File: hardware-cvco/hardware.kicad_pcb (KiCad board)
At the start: 4 copper layers, 2 parts, among them J1 Conn_Coaxial, Y1 CVCO55

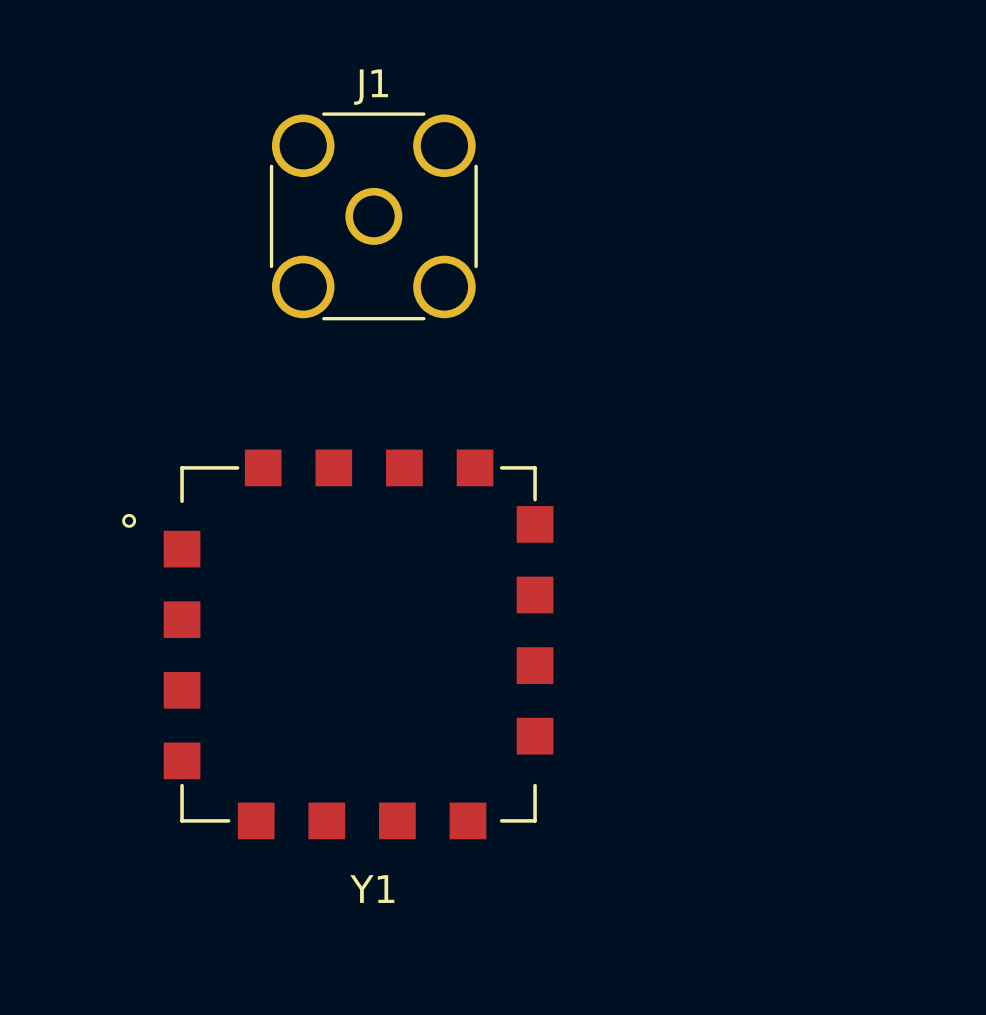
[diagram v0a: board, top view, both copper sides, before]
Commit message: 500-1000 MHz & 1000-2000 MHz Crystek VCOs.
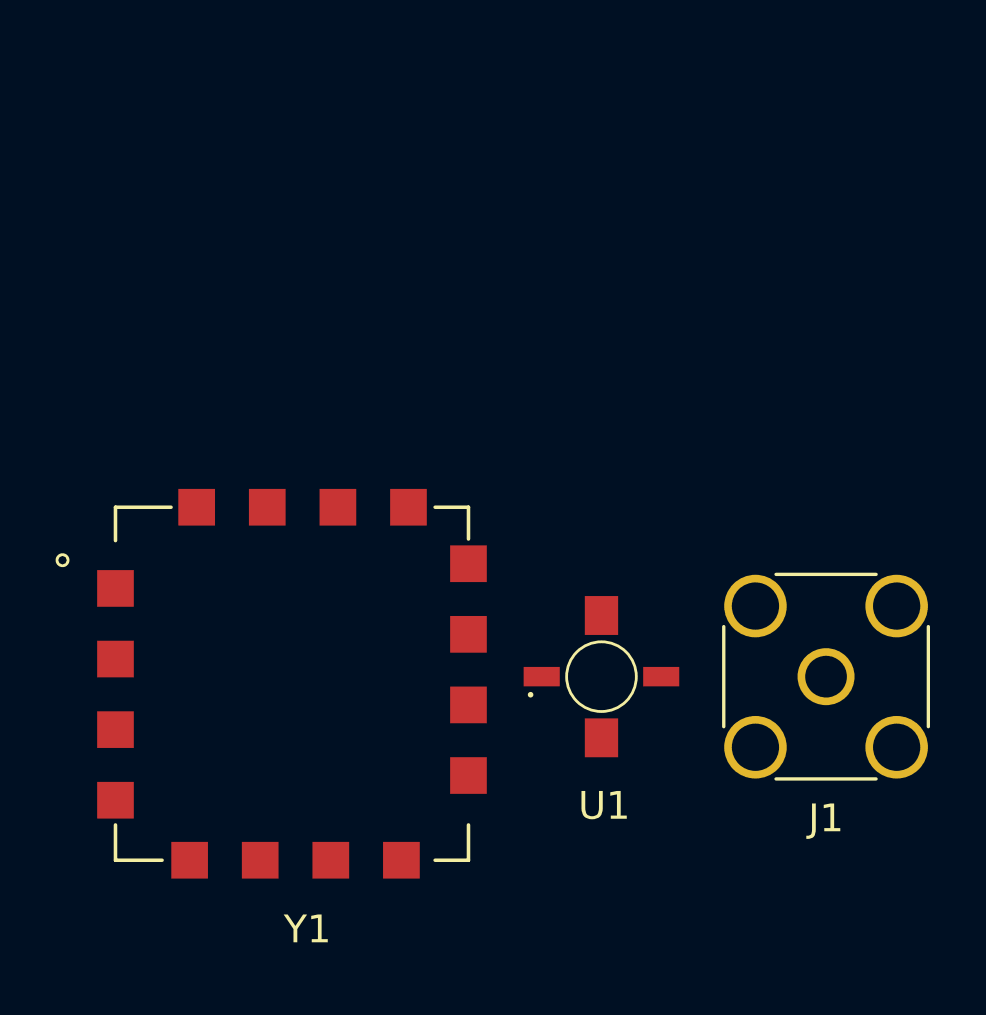
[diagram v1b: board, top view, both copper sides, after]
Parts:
- added U1: NLB-310-T1, CVCO:Micro-X-4, F.Cu at (131.4, 68.0)
- J1: value Conn_Coaxial -> SMA
- moved J1 23.2 mm to (139.5, 68.0), turned to 270 degrees
- moved Y1 2.78 mm to (113.9, 74.6)
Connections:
- J1 pad 2: Net-(J1-Pad2) -> GND
- Y1 pad 14: Net-(Y1-Pad14) -> GND

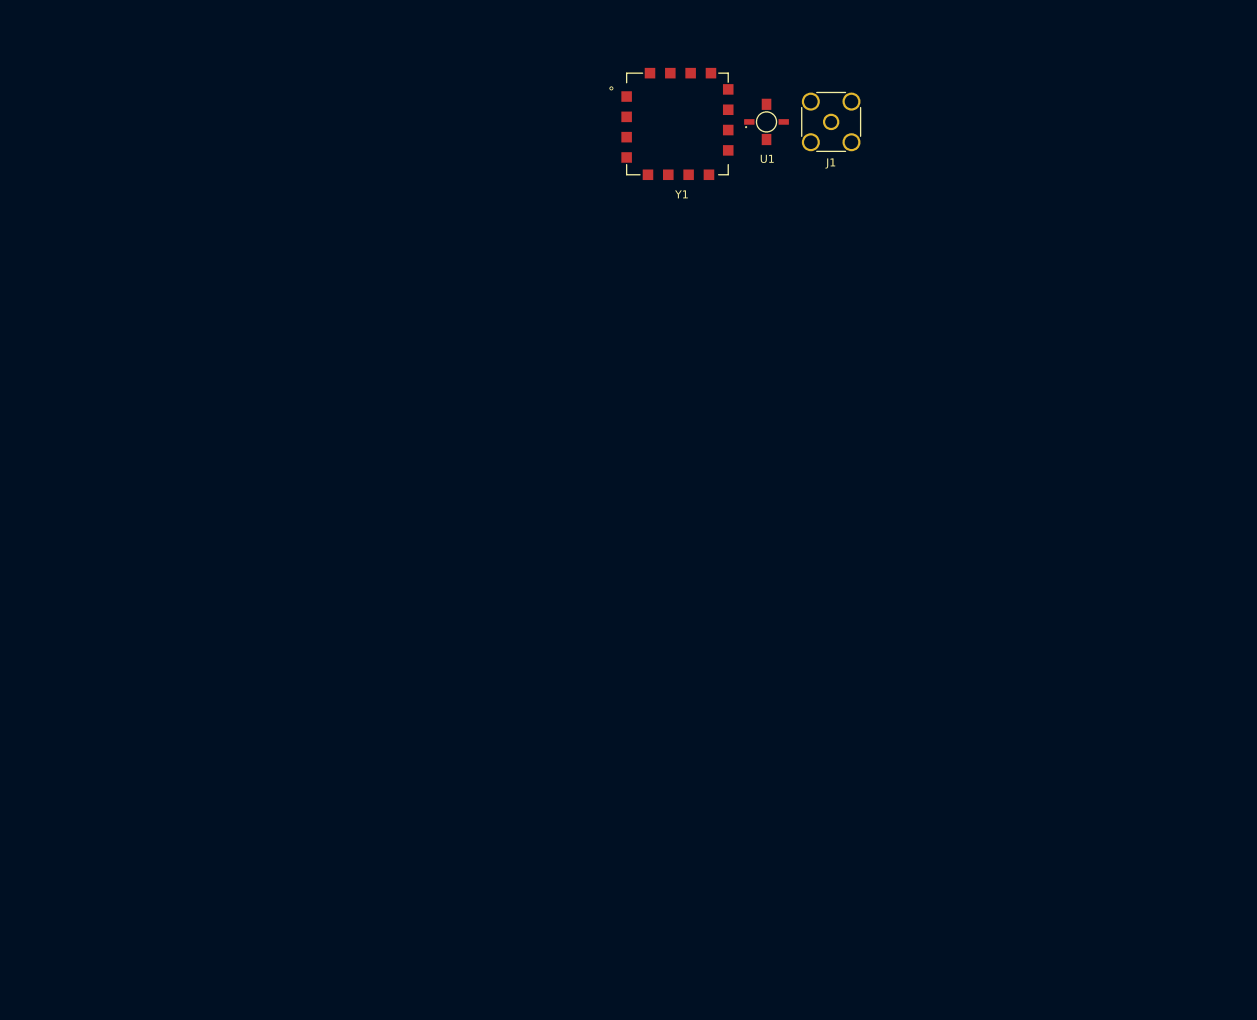
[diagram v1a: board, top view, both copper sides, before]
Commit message: Simplified CVCO design.
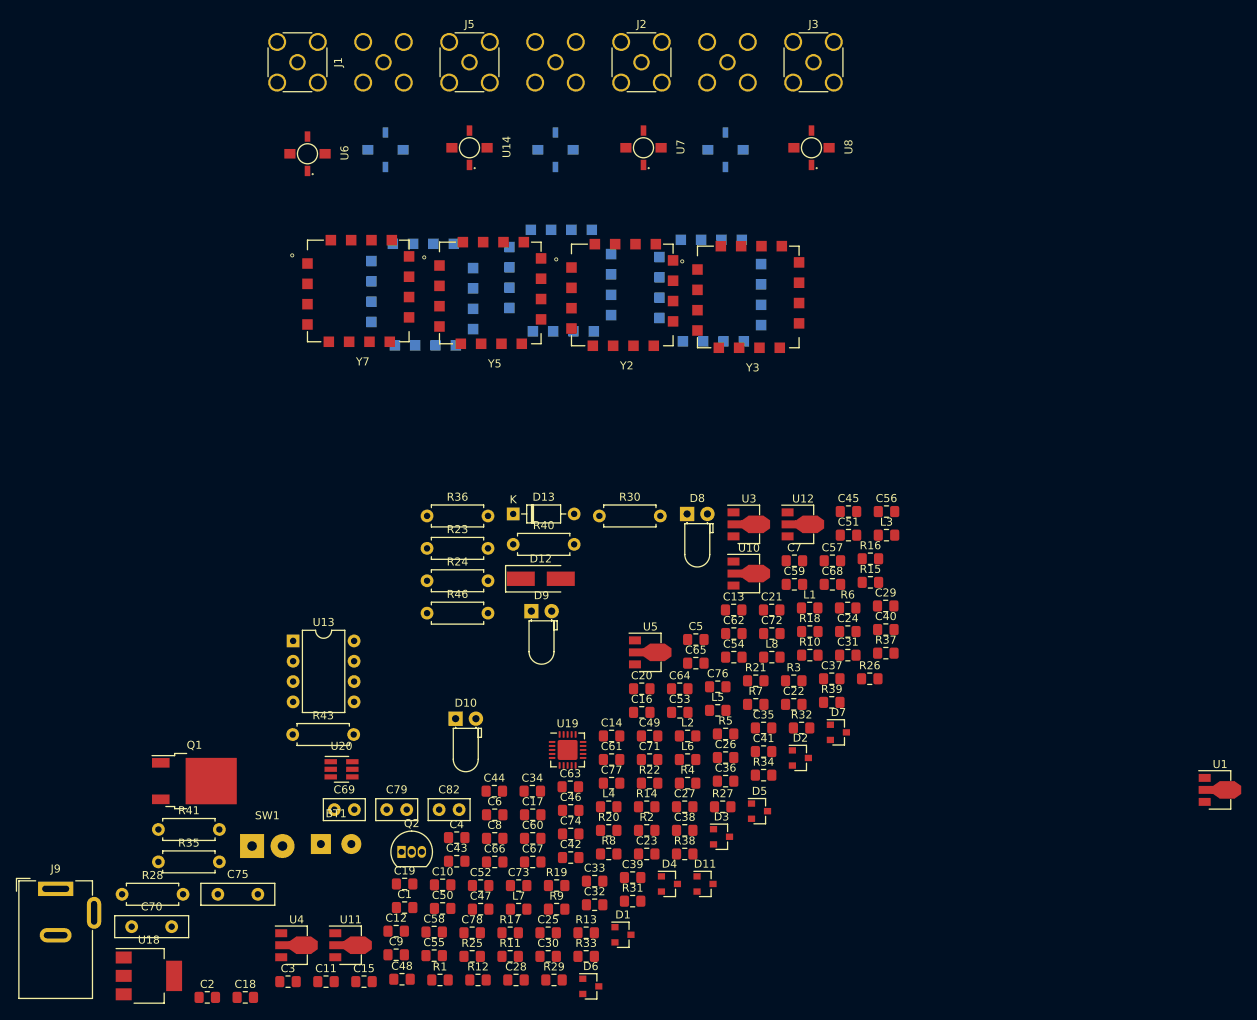
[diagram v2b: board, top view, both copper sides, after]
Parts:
- added BT1: 3.7V, Connector_Wire:SolderWirePad_1x02_P3.81mm_Drill1mm, F.Cu at (75.7, 158.3)
- added C1: 1μ, Capacitor_SMD:C_0805_2012Metric_Pad1.15x1.40mm_HandSolder, F.Cu at (86.1, 166.2)
- added C10: 0.1n, Capacitor_SMD:C_0805_2012Metric_Pad1.15x1.40mm_HandSolder, F.Cu at (90.9, 163.4)
- added C11: 1n, Capacitor_SMD:C_0805_2012Metric_Pad1.15x1.40mm_HandSolder, F.Cu at (76.3, 175.5)
- added C12: 0.1n, Capacitor_SMD:C_0805_2012Metric_Pad1.15x1.40mm_HandSolder, F.Cu at (85.1, 169.2)
- added C13: 1n, Capacitor_SMD:C_0805_2012Metric_Pad1.15x1.40mm_HandSolder, F.Cu at (127.3, 129.0)
- added C14: 0.1n, Capacitor_SMD:C_0805_2012Metric_Pad1.15x1.40mm_HandSolder, F.Cu at (112.0, 144.8)
- added C15: 1n, Capacitor_SMD:C_0805_2012Metric_Pad1.15x1.40mm_HandSolder, F.Cu at (81.1, 175.5)
- added C16: 0.1n, Capacitor_SMD:C_0805_2012Metric_Pad1.15x1.40mm_HandSolder, F.Cu at (115.8, 141.8)
- added C17: 0.1n, Capacitor_SMD:C_0805_2012Metric_Pad1.15x1.40mm_HandSolder, F.Cu at (102.2, 154.6)
- added C18: 1n, Capacitor_SMD:C_0805_2012Metric_Pad1.15x1.40mm_HandSolder, F.Cu at (66.2, 177.5)
- added C19: 0.1n, Capacitor_SMD:C_0805_2012Metric_Pad1.15x1.40mm_HandSolder, F.Cu at (86.1, 163.3)
- added C2: 0.1u, Capacitor_SMD:C_0805_2012Metric_Pad1.15x1.40mm_HandSolder, F.Cu at (61.5, 177.5)
- added C20: 1n, Capacitor_SMD:C_0805_2012Metric_Pad1.15x1.40mm_HandSolder, F.Cu at (115.8, 138.9)
- added C21: 0.1n, Capacitor_SMD:C_0805_2012Metric_Pad1.15x1.40mm_HandSolder, F.Cu at (132.0, 129.0)
- added C22: 1n, Capacitor_SMD:C_0805_2012Metric_Pad1.15x1.40mm_HandSolder, F.Cu at (134.8, 140.8)
- added C23: 0.1n, Capacitor_SMD:C_0805_2012Metric_Pad1.15x1.40mm_HandSolder, F.Cu at (116.4, 159.5)
- added C24: 1n, Capacitor_SMD:C_0805_2012Metric_Pad1.15x1.40mm_HandSolder, F.Cu at (141.5, 131.7)
- added C25: 470pF, Capacitor_SMD:C_0805_2012Metric_Pad1.15x1.40mm_HandSolder, F.Cu at (104.1, 169.4)
- added C26: 220pF, Capacitor_SMD:C_0805_2012Metric_Pad1.15x1.40mm_HandSolder, F.Cu at (126.3, 147.5)
- added C27: 100pF, Capacitor_SMD:C_0805_2012Metric_Pad1.15x1.40mm_HandSolder, F.Cu at (121.2, 153.6)
- added C28: 47pF, Capacitor_SMD:C_0805_2012Metric_Pad1.15x1.40mm_HandSolder, F.Cu at (100.1, 175.3)
- added C29: 1n, Capacitor_SMD:C_0805_2012Metric_Pad1.15x1.40mm_HandSolder, F.Cu at (146.3, 128.5)
- added C3: 1μ, Capacitor_SMD:C_0805_2012Metric_Pad1.15x1.40mm_HandSolder, F.Cu at (71.6, 175.5)
- added C30: 0.1n, Capacitor_SMD:C_0805_2012Metric_Pad1.15x1.40mm_HandSolder, F.Cu at (104.1, 172.3)
- added C31: 1n, Capacitor_SMD:C_0805_2012Metric_Pad1.15x1.40mm_HandSolder, F.Cu at (141.5, 134.7)
- added C32: 0.1n, Capacitor_SMD:C_0805_2012Metric_Pad1.15x1.40mm_HandSolder, F.Cu at (109.9, 165.9)
- added C33: 1n, Capacitor_SMD:C_0805_2012Metric_Pad1.15x1.40mm_HandSolder, F.Cu at (109.9, 162.9)
- added C34: 0.1n, Capacitor_SMD:C_0805_2012Metric_Pad1.15x1.40mm_HandSolder, F.Cu at (102.1, 151.7)
- added C35: 1n, Capacitor_SMD:C_0805_2012Metric_Pad1.15x1.40mm_HandSolder, F.Cu at (131.0, 143.8)
- added C36: 0.1n, Capacitor_SMD:C_0805_2012Metric_Pad1.15x1.40mm_HandSolder, F.Cu at (126.3, 150.4)
- added C37: 1μ, Capacitor_SMD:C_0805_2012Metric_Pad1.15x1.40mm_HandSolder, F.Cu at (139.5, 137.6)
- added C38: 0.1u, Capacitor_SMD:C_0805_2012Metric_Pad1.15x1.40mm_HandSolder, F.Cu at (121.2, 156.6)
- added C39: 1μ, Capacitor_SMD:C_0805_2012Metric_Pad1.15x1.40mm_HandSolder, F.Cu at (114.6, 162.5)
- added C4: 0.1u, Capacitor_SMD:C_0805_2012Metric_Pad1.15x1.40mm_HandSolder, F.Cu at (92.7, 157.5)
- added C40: 0.1u, Capacitor_SMD:C_0805_2012Metric_Pad1.15x1.40mm_HandSolder, F.Cu at (146.3, 131.5)
- added C41: 1μ, Capacitor_SMD:C_0805_2012Metric_Pad1.15x1.40mm_HandSolder, F.Cu at (131.0, 146.7)
- added C42: 0.1u, Capacitor_SMD:C_0805_2012Metric_Pad1.15x1.40mm_HandSolder, F.Cu at (106.9, 160.0)
- added C43: 1μF, Capacitor_SMD:C_0805_2012Metric_Pad1.15x1.40mm_HandSolder, F.Cu at (92.7, 160.4)
- added C44: 0.1μF, Capacitor_SMD:C_0805_2012Metric_Pad1.15x1.40mm_HandSolder, F.Cu at (97.4, 151.7)
- added C45: 1μF, Capacitor_SMD:C_0805_2012Metric_Pad1.15x1.40mm_HandSolder, F.Cu at (141.6, 116.7)
- added C46: 0.1μF, Capacitor_SMD:C_0805_2012Metric_Pad1.15x1.40mm_HandSolder, F.Cu at (106.9, 154.1)
- added C47: 1n, Capacitor_SMD:C_0805_2012Metric_Pad1.15x1.40mm_HandSolder, F.Cu at (95.6, 166.4)
- added C48: 0.1n, Capacitor_SMD:C_0805_2012Metric_Pad1.15x1.40mm_HandSolder, F.Cu at (85.8, 175.2)
- added C49: 1n, Capacitor_SMD:C_0805_2012Metric_Pad1.15x1.40mm_HandSolder, F.Cu at (116.8, 144.8)
- added C5: 1μ, Capacitor_SMD:C_0805_2012Metric_Pad1.15x1.40mm_HandSolder, F.Cu at (122.5, 132.7)
- added C50: 0.1n, Capacitor_SMD:C_0805_2012Metric_Pad1.15x1.40mm_HandSolder, F.Cu at (90.9, 166.3)
- added C51: 1n, Capacitor_SMD:C_0805_2012Metric_Pad1.15x1.40mm_HandSolder, F.Cu at (141.6, 119.7)
- added C52: 0.1n, Capacitor_SMD:C_0805_2012Metric_Pad1.15x1.40mm_HandSolder, F.Cu at (95.6, 163.5)
- added C53: 0.1n, Capacitor_SMD:C_0805_2012Metric_Pad1.15x1.40mm_HandSolder, F.Cu at (120.5, 141.8)
- added C54: 1n, Capacitor_SMD:C_0805_2012Metric_Pad1.15x1.40mm_HandSolder, F.Cu at (127.3, 134.9)
- added C55: 0.1n, Capacitor_SMD:C_0805_2012Metric_Pad1.15x1.40mm_HandSolder, F.Cu at (89.8, 172.2)
- added C56: 1n, Capacitor_SMD:C_0805_2012Metric_Pad1.15x1.40mm_HandSolder, F.Cu at (146.4, 116.7)
- added C57: 0.1n, Capacitor_SMD:C_0805_2012Metric_Pad1.15x1.40mm_HandSolder, F.Cu at (139.6, 122.9)
- added C58: 1n, Capacitor_SMD:C_0805_2012Metric_Pad1.15x1.40mm_HandSolder, F.Cu at (89.8, 169.3)
- added C59: 33pF, Capacitor_SMD:C_0805_2012Metric_Pad1.15x1.40mm_HandSolder, F.Cu at (134.9, 125.8)
- added C6: 0.1u, Capacitor_SMD:C_0805_2012Metric_Pad1.15x1.40mm_HandSolder, F.Cu at (97.4, 154.6)
- added C60: 27pF, Capacitor_SMD:C_0805_2012Metric_Pad1.15x1.40mm_HandSolder, F.Cu at (102.2, 157.6)
- added C61: 22pF, Capacitor_SMD:C_0805_2012Metric_Pad1.15x1.40mm_HandSolder, F.Cu at (112.0, 147.7)
- added C62: 1n, Capacitor_SMD:C_0805_2012Metric_Pad1.15x1.40mm_HandSolder, F.Cu at (127.3, 132.0)
- added C63: 0.1n, Capacitor_SMD:C_0805_2012Metric_Pad1.15x1.40mm_HandSolder, F.Cu at (106.9, 151.1)
- added C64: 1n, Capacitor_SMD:C_0805_2012Metric_Pad1.15x1.40mm_HandSolder, F.Cu at (120.5, 138.9)
- added C65: 0.1n, Capacitor_SMD:C_0805_2012Metric_Pad1.15x1.40mm_HandSolder, F.Cu at (122.5, 135.7)
- added C66: 1n, Capacitor_SMD:C_0805_2012Metric_Pad1.15x1.40mm_HandSolder, F.Cu at (97.4, 160.5)
- added C67: 0.1n, Capacitor_SMD:C_0805_2012Metric_Pad1.15x1.40mm_HandSolder, F.Cu at (102.2, 160.5)
- added C68: 10μF, Capacitor_SMD:C_0805_2012Metric_Pad1.15x1.40mm_HandSolder, F.Cu at (139.6, 125.8)
- added C69: 1nF, Capacitor_THT:C_Disc_D5.0mm_W2.5mm_P2.50mm, F.Cu at (77.4, 154.0)
- added C7: 1μ, Capacitor_SMD:C_0805_2012Metric_Pad1.15x1.40mm_HandSolder, F.Cu at (134.9, 122.9)
- added C70: 220nF, Capacitor_THT:C_Disc_D9.0mm_W2.5mm_P5.00mm, F.Cu at (52.0, 168.6)
- added C71: 4.7μF, Capacitor_SMD:C_0805_2012Metric_Pad1.15x1.40mm_HandSolder, F.Cu at (116.8, 147.7)
- added C72: 4.7μF, Capacitor_SMD:C_0805_2012Metric_Pad1.15x1.40mm_HandSolder, F.Cu at (132.0, 132.0)
- added C73: 0.1μF, Capacitor_SMD:C_0805_2012Metric_Pad1.15x1.40mm_HandSolder, F.Cu at (100.4, 163.5)
- added C74: 1μF, Capacitor_SMD:C_0805_2012Metric_Pad1.15x1.40mm_HandSolder, F.Cu at (106.9, 157.0)
- added C75: 220nF, Capacitor_THT:C_Disc_D9.0mm_W2.5mm_P5.00mm, F.Cu at (62.8, 164.6)
- added C76: 4.7μF, Capacitor_SMD:C_0805_2012Metric_Pad1.15x1.40mm_HandSolder, F.Cu at (125.3, 138.6)
- added C77: 10μF, Capacitor_SMD:C_0805_2012Metric_Pad1.15x1.40mm_HandSolder, F.Cu at (112.0, 150.7)
- added C78: 4.7μF, Capacitor_SMD:C_0805_2012Metric_Pad1.15x1.40mm_HandSolder, F.Cu at (94.6, 169.4)
- added C79: 0.1uF, Capacitor_THT:C_Disc_D5.0mm_W2.5mm_P2.50mm, F.Cu at (83.9, 154.0)
- added C8: 0.1u, Capacitor_SMD:C_0805_2012Metric_Pad1.15x1.40mm_HandSolder, F.Cu at (97.4, 157.6)
- added C82: 0.1uF, Capacitor_THT:C_Disc_D5.0mm_W2.5mm_P2.50mm, F.Cu at (90.5, 154.0)
- added C9: 1n, Capacitor_SMD:C_0805_2012Metric_Pad1.15x1.40mm_HandSolder, F.Cu at (85.1, 172.1)
- added D1: 5V, Package_TO_SOT_SMD:SOT-23, F.Cu at (113.4, 169.6)
- added D10: Yellow, LED_THT:LED_D3.0mm_Horizontal_O1.27mm_Z2.0mm, F.Cu at (92.5, 142.6)
- added D11: 3V, Package_TO_SOT_SMD:SOT-23, F.Cu at (123.7, 163.3)
- added D12: 1N4002, Diode_SMD:D_SMA_Handsoldering, F.Cu at (103.2, 125.1)
- added D13: 10V, Diode_THT:D_DO-35_SOD27_P7.62mm_Horizontal, F.Cu at (99.7, 117.0)
- added D2: 18V, Package_TO_SOT_SMD:SOT-23, F.Cu at (135.6, 147.5)
- added D3: 18V, Package_TO_SOT_SMD:SOT-23, F.Cu at (125.8, 157.4)
- added D4: 20V, Package_TO_SOT_SMD:SOT-23, F.Cu at (119.2, 163.3)
- added D5: 20V, Package_TO_SOT_SMD:SOT-23, F.Cu at (130.5, 154.2)
- added D6: 16V, Package_TO_SOT_SMD:SOT-23, F.Cu at (109.4, 176.1)
- added D7: 20V, Package_TO_SOT_SMD:SOT-23, F.Cu at (140.4, 144.3)
- added D8: Green, LED_THT:LED_D3.0mm_Horizontal_O1.27mm_Z2.0mm, F.Cu at (121.5, 117.0)
- added D9: Red, LED_THT:LED_D3.0mm_Horizontal_O1.27mm_Z2.0mm, F.Cu at (102.0, 129.2)
- added J2: SMA, Connector_Coaxial:SMA_Amphenol_132134_Vertical, F.Cu at (115.8, 60.6)
- added J3: SMA, Connector_Coaxial:SMA_Amphenol_132134_Vertical, F.Cu at (137.2, 60.6)
- added J4: SMA, Connector_Coaxial:SMA_Amphenol_132134_Vertical, B.Cu at (83.5, 60.6)
- added J5: SMA, Connector_Coaxial:SMA_Amphenol_132134_Vertical, F.Cu at (94.2, 60.6)
- added J6: SMA, Connector_Coaxial:SMA_Amphenol_132134_Vertical, B.Cu at (126.5, 60.6)
- added J7: SMA, Connector_Coaxial:SMA_Amphenol_132134_Vertical, B.Cu at (105.0, 60.6)
- added J9: DC, Connector_BarrelJack:BarrelJack_Wuerth_6941xx301002, F.Cu at (42.5, 163.9)
- added L1: 470n, Inductor_SMD:L_0805_2012Metric_Pad1.15x1.40mm_HandSolder, F.Cu at (136.8, 128.8)
- added L2: 470n, Inductor_SMD:L_0805_2012Metric_Pad1.15x1.40mm_HandSolder, F.Cu at (121.5, 144.8)
- added L3: 470n, Inductor_SMD:L_0805_2012Metric_Pad1.15x1.40mm_HandSolder, F.Cu at (146.4, 119.7)
- added L4: 470n, Inductor_SMD:L_0805_2012Metric_Pad1.15x1.40mm_HandSolder, F.Cu at (111.7, 153.6)
- added L5: 470n, Inductor_SMD:L_0805_2012Metric_Pad1.15x1.40mm_HandSolder, F.Cu at (125.3, 141.6)
- added L6: 470n, Inductor_SMD:L_0805_2012Metric_Pad1.15x1.40mm_HandSolder, F.Cu at (121.5, 147.7)
- added L7: 470n, Inductor_SMD:L_0805_2012Metric_Pad1.15x1.40mm_HandSolder, F.Cu at (100.4, 166.4)
- added L8: 10μH, Capacitor_SMD:C_0805_2012Metric_Pad1.15x1.40mm_HandSolder, F.Cu at (132.0, 134.9)
- added Q1: AOD403, Package_TO_SOT_SMD:TO-252-2, F.Cu at (59.9, 150.4)
- added Q2: PN2222A, Package_TO_SOT_THT:TO-92_Inline, F.Cu at (85.8, 159.3)
- added R1: 1k, Resistor_SMD:R_0805_2012Metric_Pad1.15x1.40mm_HandSolder, F.Cu at (90.6, 175.3)
- added R10: 560, Resistor_SMD:R_0805_2012Metric_Pad1.15x1.40mm_HandSolder, F.Cu at (136.8, 134.7)
- added R11: 680, Resistor_SMD:R_0805_2012Metric_Pad1.15x1.40mm_HandSolder, F.Cu at (99.3, 172.3)
- added R12: 470, Resistor_SMD:R_0805_2012Metric_Pad1.15x1.40mm_HandSolder, F.Cu at (95.3, 175.3)
- added R13: 1k, Resistor_SMD:R_0805_2012Metric_Pad1.15x1.40mm_HandSolder, F.Cu at (108.8, 169.4)
- added R14: 1k, Resistor_SMD:R_0805_2012Metric_Pad1.15x1.40mm_HandSolder, F.Cu at (116.4, 153.6)
- added R15: 1k, Resistor_SMD:R_0805_2012Metric_Pad1.15x1.40mm_HandSolder, F.Cu at (144.4, 125.6)
- added R16: 82, Resistor_SMD:R_0805_2012Metric_Pad1.15x1.40mm_HandSolder, F.Cu at (144.4, 122.6)
- added R17: 120, Resistor_SMD:R_0805_2012Metric_Pad1.15x1.40mm_HandSolder, F.Cu at (99.3, 169.4)
- added R18: 150, Resistor_SMD:R_0805_2012Metric_Pad1.15x1.40mm_HandSolder, F.Cu at (136.8, 131.7)
- added R19: 220, Resistor_SMD:R_0805_2012Metric_Pad1.15x1.40mm_HandSolder, F.Cu at (105.1, 163.5)
- added R2: 1k, Resistor_SMD:R_0805_2012Metric_Pad1.15x1.40mm_HandSolder, F.Cu at (116.4, 156.6)
- added R20: 270, Resistor_SMD:R_0805_2012Metric_Pad1.15x1.40mm_HandSolder, F.Cu at (111.7, 156.6)
- added R21: 470, Resistor_SMD:R_0805_2012Metric_Pad1.15x1.40mm_HandSolder, F.Cu at (130.0, 137.9)
- added R22: 10k, Resistor_SMD:R_0805_2012Metric_Pad1.15x1.40mm_HandSolder, F.Cu at (116.8, 150.7)
- added R23: 4.7k, Resistor_THT:R_Axial_DIN0207_L6.3mm_D2.5mm_P7.62mm_Horizontal, F.Cu at (88.9, 121.3)
- added R24: 10k, Resistor_THT:R_Axial_DIN0207_L6.3mm_D2.5mm_P7.62mm_Horizontal, F.Cu at (88.9, 125.4)
- added R25: 120, Resistor_SMD:R_0805_2012Metric_Pad1.15x1.40mm_HandSolder, F.Cu at (94.6, 172.3)
- added R26: 120, Resistor_SMD:R_0805_2012Metric_Pad1.15x1.40mm_HandSolder, F.Cu at (144.3, 137.6)
- added R27: 120, Resistor_SMD:R_0805_2012Metric_Pad1.15x1.40mm_HandSolder, F.Cu at (125.9, 153.6)
- added R28: 15k, Resistor_THT:R_Axial_DIN0207_L6.3mm_D2.5mm_P7.62mm_Horizontal, F.Cu at (50.8, 164.6)
- added R29: 4.7k, Resistor_SMD:R_0805_2012Metric_Pad1.15x1.40mm_HandSolder, F.Cu at (104.8, 175.3)
- added R3: 1k, Resistor_SMD:R_0805_2012Metric_Pad1.15x1.40mm_HandSolder, F.Cu at (134.8, 137.9)
- added R30: 100k, Resistor_THT:R_Axial_DIN0207_L6.3mm_D2.5mm_P7.62mm_Horizontal, F.Cu at (110.5, 117.3)
- added R31: 3M, Resistor_SMD:R_0805_2012Metric_Pad1.15x1.40mm_HandSolder, F.Cu at (114.6, 165.4)
- added R32: 10k, Resistor_SMD:R_0805_2012Metric_Pad1.15x1.40mm_HandSolder, F.Cu at (135.8, 143.8)
- added R33: 1k, Resistor_SMD:R_0805_2012Metric_Pad1.15x1.40mm_HandSolder, F.Cu at (108.8, 172.3)
- added R34: 10k, Resistor_SMD:R_0805_2012Metric_Pad1.15x1.40mm_HandSolder, F.Cu at (131.0, 149.7)
- added R35: 10k, Resistor_THT:R_Axial_DIN0207_L6.3mm_D2.5mm_P7.62mm_Horizontal, F.Cu at (55.4, 160.5)
- added R36: 10k, Resistor_THT:R_Axial_DIN0207_L6.3mm_D2.5mm_P7.62mm_Horizontal, F.Cu at (88.9, 117.3)
- added R37: 100k, Resistor_SMD:R_0805_2012Metric_Pad1.15x1.40mm_HandSolder, F.Cu at (146.3, 134.4)
- added R38: 10k, Resistor_SMD:R_0805_2012Metric_Pad1.15x1.40mm_HandSolder, F.Cu at (121.2, 159.5)
- added R39: 100k, Resistor_SMD:R_0805_2012Metric_Pad1.15x1.40mm_HandSolder, F.Cu at (139.5, 140.6)
- added R4: 1k, Resistor_SMD:R_0805_2012Metric_Pad1.15x1.40mm_HandSolder, F.Cu at (121.5, 150.7)
- added R40: 15k, Resistor_THT:R_Axial_DIN0207_L6.3mm_D2.5mm_P7.62mm_Horizontal, F.Cu at (99.7, 120.8)
- added R41: 15k, Resistor_THT:R_Axial_DIN0207_L6.3mm_D2.5mm_P7.62mm_Horizontal, F.Cu at (55.4, 156.5)
- added R43: 100, Resistor_THT:R_Axial_DIN0207_L6.3mm_D2.5mm_P7.62mm_Horizontal, F.Cu at (72.2, 144.6)
- added R46: 2k, Resistor_THT:R_Axial_DIN0207_L6.3mm_D2.5mm_P7.62mm_Horizontal, F.Cu at (88.9, 129.4)
- added R5: 82, Resistor_SMD:R_0805_2012Metric_Pad1.15x1.40mm_HandSolder, F.Cu at (126.3, 144.5)
- added R6: 180, Resistor_SMD:R_0805_2012Metric_Pad1.15x1.40mm_HandSolder, F.Cu at (141.5, 128.8)
- added R7: 180, Resistor_SMD:R_0805_2012Metric_Pad1.15x1.40mm_HandSolder, F.Cu at (130.0, 140.8)
- added R8: 150, Resistor_SMD:R_0805_2012Metric_Pad1.15x1.40mm_HandSolder, F.Cu at (111.7, 159.5)
- added R9: 220, Resistor_SMD:R_0805_2012Metric_Pad1.15x1.40mm_HandSolder, F.Cu at (105.1, 166.4)
- added SW1: On/Off, Connector_Wire:SolderWirePad_1x02_P3.81mm_Drill1.2mm, F.Cu at (67.1, 158.5)
- added U10: L78L05_SOT89, Package_TO_SOT_SMD:SOT-89-3, F.Cu at (128.7, 124.5)
- added U11: L78L08_SOT89, Package_TO_SOT_SMD:SOT-89-3, F.Cu at (79.0, 170.9)
- added U12: L78L10_SOT89, Package_TO_SOT_SMD:SOT-89-3, F.Cu at (135.5, 118.3)
- added U13: PIC12F675-ISN, Package_DIP:DIP-8_W7.62mm, F.Cu at (72.2, 132.9)
- added U14: NLB-310-T1, CVCO:Micro-X-4, F.Cu at (94.2, 71.2)
- added U15: NLB-310-T1, CVCO:Micro-X-4, B.Cu at (126.2, 71.5)
- added U16: NLB-310-T1, CVCO:Micro-X-4, B.Cu at (105.0, 71.5)
- added U18: LM317DCYR, Package_TO_SOT_SMD:SOT-223-3_TabPin2, F.Cu at (54.2, 174.8)
- added U19: MCP73871-2AA, Package_DFN_QFN:QFN-20-1EP_4x4mm_P0.5mm_EP2.5x2.5mm, F.Cu at (106.5, 146.5)
- added U20: TPS61046, Package_TO_SOT_SMD:SOT-23-6_Handsoldering, F.Cu at (78.3, 148.9)
- added U3: L78L12_SOT89, Package_TO_SOT_SMD:SOT-89-3, F.Cu at (128.7, 118.3)
- added U4: L78L12_SOT89, Package_TO_SOT_SMD:SOT-89-3, F.Cu at (72.2, 170.9)
- added U5: L78L10_SOT89, Package_TO_SOT_SMD:SOT-89-3, F.Cu at (116.4, 134.3)
- added U6: NLB-310-T1, CVCO:Micro-X-4, F.Cu at (74.0, 72.0)
- added U7: NLB-310-T1, CVCO:Micro-X-4, F.Cu at (116.0, 71.2)
- added U8: NLB-310-T1, CVCO:Micro-X-4, F.Cu at (137.0, 71.2)
- added U9: NLB-310-T1, CVCO:Micro-X-4, B.Cu at (83.8, 71.5)
- added Y2: CVCO55CW-0200-0500, CVCO:CVCO55, F.Cu at (107.0, 96.0)
- added Y3: CV55CW500-1000, CVCO:CVCO55, F.Cu at (122.8, 96.2)
- added Y4: CVCO55CW-1000-2000, CVCO:CVCO55, B.Cu at (99.2, 81.5)
- added Y5: CV55BE1600-3200, CVCO:CVCO55, F.Cu at (90.5, 95.8)
- added Y6: CVCO55CC-3180-3710, CVCO:CVCO55, B.Cu at (82.0, 83.2)
- added Y7: CVCO55CW-3500-4500, CVCO:CVCO55, F.Cu at (74.0, 95.5)
- U1: value NLB-310-T1 -> L78L05_SOT89; footprint CVCO:Micro-X-4 -> Package_TO_SOT_SMD:SOT-89-3
- Y1: value CVCO55 -> CVCO55CW-0100-0200; moved to B.Cu
- moved U1 100.7 mm to (187.6, 151.5)
- moved J1 67.1 mm to (72.8, 60.6), turned to 0 degrees
- moved Y1 9.10 mm to (118.0, 82.8)
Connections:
- J1 pad 2: GND -> P2_VSS
- U1 pad 1: Net-(C5-Pad1) -> VCC_1
- U1 pad 2: GND -> P2_VSS
- U1 pad 3: Net-(J1-Pad1) -> P2_VDD
- Y1 pad 1: GND -> P2_VSS
- Y1 pad 11: GND -> P2_VSS
- Y1 pad 12: GND -> P2_VSS
- Y1 pad 13: GND -> P2_VSS
- Y1 pad 14: GND -> Net-(R9-Pad2)
- Y1 pad 15: GND -> P2_VSS
- Y1 pad 16: GND -> P2_VSS
- Y1 pad 2: Net-(C1-Pad1) -> VT_1
- Y1 pad 3: GND -> P2_VSS
- Y1 pad 4: GND -> P2_VSS
- Y1 pad 5: GND -> P2_VSS
- Y1 pad 6: GND -> P2_VSS
- Y1 pad 7: GND -> P2_VSS
- Y1 pad 8: GND -> P2_VSS
- Y1 pad 9: GND -> P2_VSS
